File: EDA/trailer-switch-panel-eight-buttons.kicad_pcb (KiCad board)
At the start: 2 copper layers, 113.4 x 65.8 mm, 41 parts, among them IC1 AP63203WU-7, J1 Conn_01x06, J2 Conn_01x04, SW1 SW_Push, SW2 SW_Push, SW3 SW_Push, SW4 SW_Push, SW5 SW_Push, SW6 SW_Push, SW7 SW_Push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

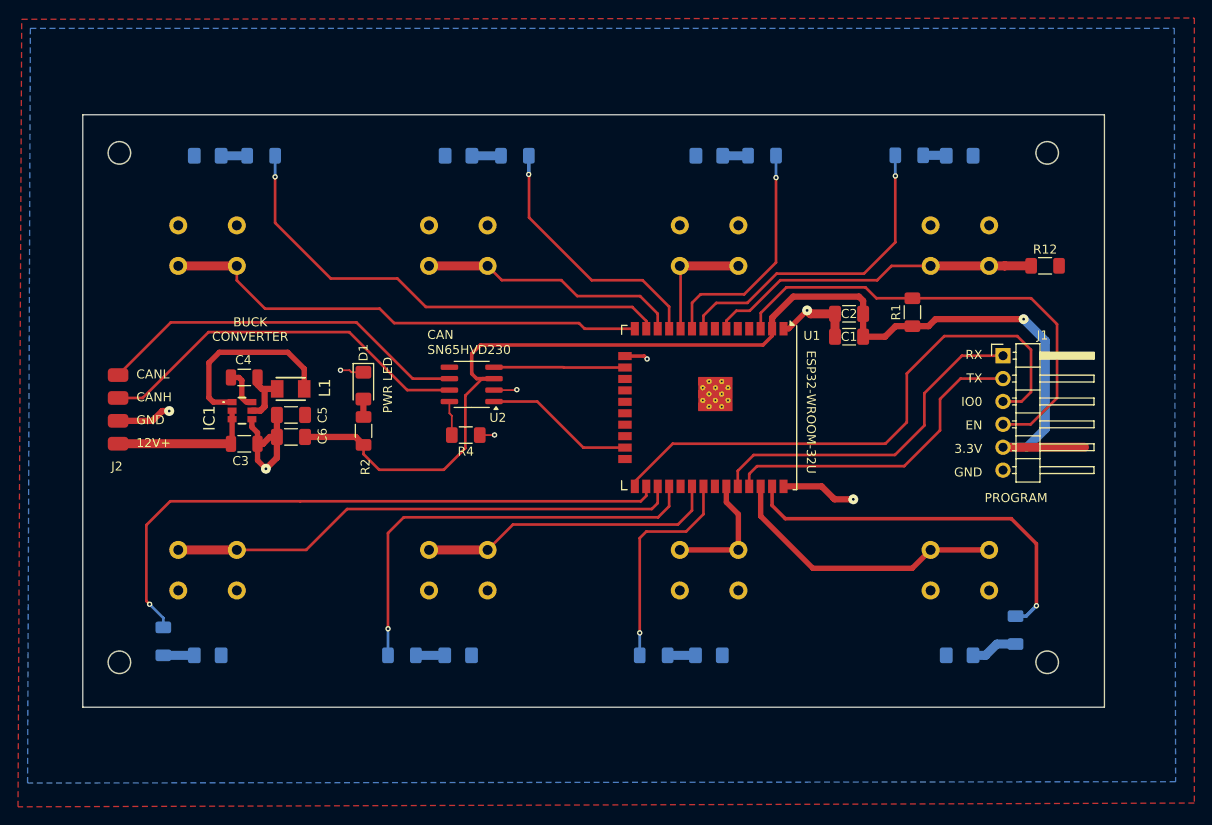
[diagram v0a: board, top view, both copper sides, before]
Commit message: Updated PCB to use JST XH connectors
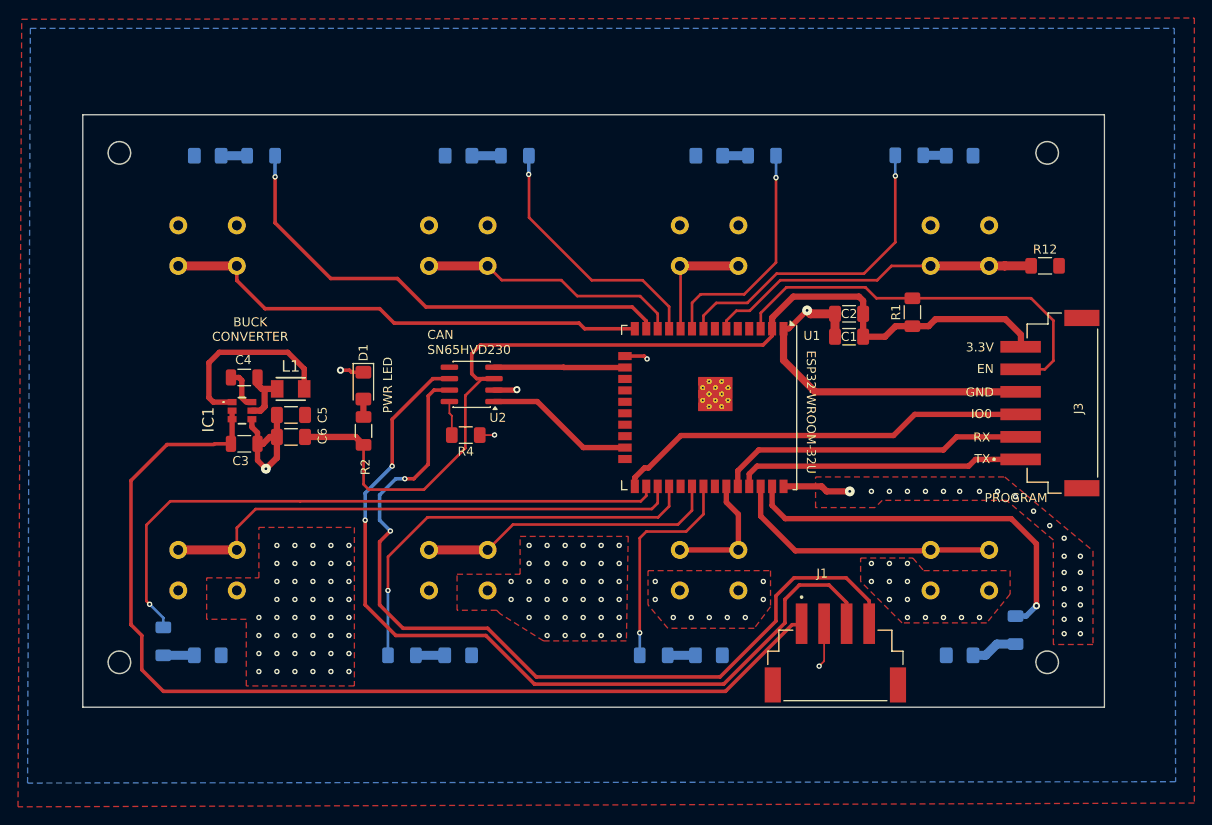
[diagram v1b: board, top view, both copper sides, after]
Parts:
- removed J2: Conn_01x04, CustomLibraries:CAN_PLUS_POWER
- added J3: S6B-XH-SM4-TB, TrailCurrentFootprints:JST_S6B-XH-SM4-TB, F.Cu at (135.6, 79.3)
- added LOGO: TrailCurrentLogo_Text, TrailCurrentFootprints:TrailCurrentLogo_Text, F.Cu at (88.2, 84.1)
- added LOGO: TrailCurrentLogo_Icon, TrailCurrentFootprints:TrailCurrentLogo_Icon, B.Cu at (85.8, 79.3)
- IC1: footprint CustomLibraries:AP63203WU7 -> TrailCurrentFootprints:AP63203WU7
- J1: value Conn_01x06 -> S4B-XH-SM4-TB; footprint Connector_PinHeader_2.54mm:PinHeader_1x06_P2.54mm_Horizontal -> TrailCurrentFootprints:JST_S4B-XH-SM4-TB
- L1: value NLV32T-3R9J-EF (3.9uH) -> NLV32T-3R9J-EF; footprint CustomLibraries:INDM3225X240N -> TrailCurrentFootprints:NLV32T-3R9J-EF
- moved J1 41.0 mm to (108.2, 110.6)
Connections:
- J1 pad 1: /RX -> +12V
- J1 pad 2: /TX -> GND
- J1 pad 3: /IO0 -> /CANL
- J1 pad 4: /EN -> /CANH
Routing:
- net +12V: track 16.3 -> 115.3 mm
- net /CANH: track 42.5 -> 97.8 mm, vias 0 -> 2
- net /CANL: track 41.8 -> 96.5 mm, vias 0 -> 2
- net GND: track 48.7 -> 78.0 mm, vias 8 -> 135
- net +3.3V: track 154.6 -> 132.3 mm, vias 1 -> 0
- net /IO0: track 63.2 -> 46.8 mm
- net /EN: track 52.9 -> 45.4 mm
- net /RX: track 38.6 -> 34.7 mm
- net /TX: track 36.0 -> 32.2 mm
- net /BTN08: track 31.9 -> 30.3 mm
- net /LED6: track 48.3 -> 46.7 mm
- net /BTN05: track 57.2 -> 58.7 mm
- added copper zone on F.Cu, net GND
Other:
- board text removed: "CENTRAL SWITCH PANEL"
- board text removed: "KDEMOTORSPORTS"
- board text removed: "V1.0.1"

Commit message: Added DIP switch for CAN Termination and device ID settings
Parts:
- added R13: 120, Resistor_SMD:R_1206_3216Metric_Pad1.30x1.75mm_HandSolder, F.Cu at (61.4, 76.3)
- added R14: 10k, Resistor_SMD:R_1206_3216Metric_Pad1.30x1.75mm_HandSolder, F.Cu at (27.6, 65.4)
- added R15: 10k, Resistor_SMD:R_1206_3216Metric_Pad1.30x1.75mm_HandSolder, F.Cu at (31.4, 65.3)
- added R16: 10k, Resistor_SMD:R_1206_3216Metric_Pad1.30x1.75mm_HandSolder, F.Cu at (36.4, 83.9)
- added SW9: DS-04, TrailCurrentFootprints:DS-04, F.Cu at (31.4, 74.9)
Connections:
- U1 pad 4: unconnected-(U1-SENSOR_VP-Pad4) -> /ADDR02
- U1 pad 5: unconnected-(U1-SENSOR_VN-Pad5) -> /ADDR01
- U1 pad 7: unconnected-(U1-IO35-Pad7) -> /ADDR03
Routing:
- net /ADDR01: track 0.00 -> 125.4 mm, vias 0 -> 2
- net /ADDR03: track 0.00 -> 85.6 mm
- net /ADDR02: track 0.00 -> 82.0 mm
- net +3.3V: track 132.3 -> 194.6 mm, vias 0 -> 4
- net /CANL: track 96.5 -> 140.7 mm, vias 2 -> 4
- net Net-(R13-Pad2): track 0.00 -> 27.7 mm
- net /CANH: track 97.8 -> 101.7 mm
